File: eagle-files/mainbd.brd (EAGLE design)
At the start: 69.1 x 28 mm, 25 parts, among them J1 4328, T1 3904, X1 TSW-102-07-G-S

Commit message: Moving componets around a little bit to better accomidate xaio board
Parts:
- moved L 1.76 mm to (30.6, 1.54)
- moved R5 1.31 mm to (36.4, 5.49)
- moved 3.3V-LDO 1.26 mm to (31.5, 5.58)
- moved R3 1.04 mm to (35.6, 1.49)
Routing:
- net A2: track 11.3 -> 13.7 mm
- net D9: track 3.07 -> 4.37 mm
- net N$1: track 4.51 -> 3.24 mm
- net 5V: track 35.6 -> 36.9 mm
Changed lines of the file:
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@@
 </autorouter>
 <elements>
-<element name="L" library="adafruit" package="CHIP-LED0805" value="Red" x="29.02" y="2.38" smashed="yes" rot="R270"/>
-<element name="R3" library="adafruit" package="M0805" value="1K" x="35.49" y="2.52" smashed="yes" rot="R180">
-<attribute name="NAME" x="36.706" y="5.304" size="1.27" layer="25" rot="R180"/>
+<element name="L" library="adafruit" package="CHIP-LED0805" value="Red" x="30.564046875" y="1.537128125" smashed="yes" rot="R270"/>
+<element name="R3" library="adafruit" package="M0805" value="1K" x="35.58396875" y="1.485784375" smashed="yes" rot="R180">
+<attribute name="NAME" x="36.79996875" y="4.269784375" size="1.27" layer="25" rot="R180"/>
 </element>
 <element name="SV1" library="con-lstb" library_urn="urn:adsk.eagle:library:162" package="MA10-2" package3d_urn="urn:adsk.eagle:package:8331/1" value="" x="77.47" y="13.97" smashed="yes" rot="MR270">
@@
 </element>
 <element name="U$2" library="sjm4306_LOGO" package="SJM4306_SMALL_NO_MASK" value="" x="28.45" y="17.6" smashed="yes" rot="R45"/>
-<element name="R5" library="adafruit" package="M0805" value="10K" x="36.05" y="6.75" smashed="yes" rot="R90">
-<attribute name="NAME" x="35.034" y="5.734" size="1.27" layer="25" rot="R90"/>
-<attribute name="VALUE" x="38.336" y="5.734" size="1.27" layer="27" rot="R90"/>
+<element name="R5" library="adafruit" package="M0805" value="10K" x="36.407084375" y="5.490134375" smashed="yes" rot="R90">
+<attribute name="NAME" x="35.391084375" y="4.474134375" size="1.27" layer="25" rot="R90"/>
+<attribute name="VALUE" x="38.693084375" y="4.474134375" size="1.27" layer="27" rot="R90"/>
 </element>
 <element name="U$4" library="mgregg" package="CAP-330" value="CAP-330" x="54.4" y="2.65" smashed="yes" rot="R90"/>
@@
 </element>
 <element name="U$9" library="mgregg" package="SMA-DIODE" value="DIODE-ZENIER-CMSH1-20MLTR13" x="46.5" y="13.25" smashed="yes" rot="R270"/>
-<element name="3.3V-LDO" library="mgregg" package="SOT89-BCE" value="LDO-3.3V-AZ1117CR-3.3TRG1" x="30.612034375" y="6.514896875" smashed="yes" rot="R270">
-<attribute name="NAME" x="33.787034375" y="9.054896875" size="1.27" layer="25" rot="R270"/>
-<attribute name="VALUE" x="25.067134375" y="14.769996875" size="1.27" layer="27" rot="R270"/>
+<element name="3.3V-LDO" library="mgregg" package="SOT89-BCE" value="LDO-3.3V-AZ1117CR-3.3TRG1" x="31.454240625" y="5.578375" smashed="yes" rot="R270">
+<attribute name="NAME" x="34.629240625" y="8.118375" size="1.27" layer="25" rot="R270"/>
+<attribute name="VALUE" x="25.909340625" y="13.833475" size="1.27" layer="27" rot="R270"/>
 </element>
 </elements>
@@
 <wire x1="60.2742" y1="25.6032" x2="60.42" y2="25.5" width="0.1524" layer="16"/>
 <wire x1="46.228" y1="3.2004" x2="45.1612" y2="3.2004" width="0.1524" layer="1"/>
-<wire x1="28.076634375" y1="4.976696875" x2="28.072034375" y2="5.015896875" width="0.1524" layer="1"/>
+<wire x1="28.918840625" y1="4.040175" x2="28.914240625" y2="4.079375" width="0.1524" layer="1"/>
 <wire x1="46.228" y1="3.2004" x2="46.4" y2="3.25" width="0.1524" layer="1"/>
-<wire x1="27.898834375" y1="4.976696875" x2="28.072034375" y2="5.015896875" width="0.1524" layer="1"/>
-<wire x1="28.072034375" y1="5.015896875" x2="27.283615625" y2="5.015896875" width="0.508" layer="1"/>
-<wire x1="27.283615625" y1="5.015896875" x2="25.1263125" y2="7.1732" width="0.508" layer="1"/>
+<wire x1="28.741040625" y1="4.040175" x2="28.914240625" y2="4.079375" width="0.1524" layer="1"/>
+<wire x1="28.914240625" y1="4.079375" x2="28.2201375" y2="4.079375" width="0.508" layer="1"/>
+<wire x1="28.2201375" y1="4.079375" x2="25.1263125" y2="7.1732" width="0.508" layer="1"/>
 <wire x1="25.1263125" y1="9.6738875" x2="25.0983" y2="9.7019" width="0.508" layer="1"/>
 <via x="25.0983" y="9.7019" extent="1-16" drill="0.35"/>
@@
 <contactref element="L" pad="A"/>
 <contactref element="U$7" pad="P$8"/>
-<wire x1="27.9146" y1="3.7338" x2="27.9146" y2="2.4892" width="0.1524" layer="1"/>
-<wire x1="27.0256" y1="4.6228" x2="27.9146" y2="3.7338" width="0.1524" layer="16"/>
-<wire x1="27.0256" y1="4.8006" x2="27.0256" y2="4.6228" width="0.1524" layer="16"/>
+<wire x1="27.0256" y1="2.46931875" x2="27.259553125" y2="2.235365625" width="0.1524" layer="16"/>
+<wire x1="27.0256" y1="4.8006" x2="27.0256" y2="2.46931875" width="0.1524" layer="16"/>
 <wire x1="21.5138" y1="10.3124" x2="27.0256" y2="4.8006" width="0.1524" layer="16"/>
 <wire x1="20.9804" y1="10.3124" x2="21.5138" y2="10.3124" width="0.1524" layer="16"/>
-<wire x1="27.9146" y1="2.4892" x2="27.97" y2="2.38" width="0.1524" layer="1"/>
+<wire x1="27.259553125" y1="2.235365625" x2="28.008365625" y2="2.235365625" width="0.1524" layer="1"/>
+<wire x1="28.706603125" y1="1.537128125" x2="28.008365625" y2="2.235365625" width="0.1524" layer="1"/>
+<wire x1="29.514046875" y1="1.537128125" x2="28.706603125" y2="1.537128125" width="0.1524" layer="1"/>
 <wire x1="20.9804" y1="10.3124" x2="20.85" y2="10.46" width="0.1524" layer="16"/>
-<via x="27.9146" y="3.7338" extent="1-16" drill="0.35"/>
+<via x="27.259553125" y="2.235365625" extent="1-16" drill="0.35"/>
 </signal>
 <signal name="D2">
@@
 <contactref element="L" pad="C"/>
 <contactref element="R3" pad="2"/>
-<wire x1="34.4932" y1="2.4892" x2="30.226" y2="2.4892" width="0.1524" layer="1"/>
-<wire x1="30.226" y1="2.4892" x2="30.07" y2="2.38" width="0.1524" layer="1"/>
-<wire x1="34.4932" y1="2.4892" x2="34.54" y2="2.52" width="0.1524" layer="1"/>
+<wire x1="34.052178125" y1="1.86866875" x2="32.087678125" y2="1.86866875" width="0.1524" layer="1"/>
+<wire x1="32.087678125" y1="1.86866875" x2="31.614046875" y2="1.537128125" width="0.1524" layer="1"/>
+<wire x1="34.052178125" y1="1.86866875" x2="34.63396875" y2="1.485784375" width="0.1524" layer="1"/>
 </signal>
 <signal name="G1">
@@
 <contactref element="R5" pad="2"/>
 <contactref element="U$7" pad="P$7"/>
-<wire x1="36.0934" y1="9.0678" x2="36.0934" y2="7.8232" width="0.1524" layer="1"/>
+<wire x1="36.0934" y1="9.0678" x2="36.0934" y2="7.33059375" width="0.1524" layer="1"/>
 <wire x1="36.449" y1="9.4234" x2="36.0934" y2="9.0678" width="0.1524" layer="1"/>
 <wire x1="36.449" y1="9.9568" x2="36.449" y2="9.4234" width="0.1524" layer="1"/>
 <wire x1="36.0934" y1="10.3124" x2="36.449" y2="9.9568" width="0.1524" layer="1"/>
-<wire x1="36.0934" y1="7.8232" x2="36.05" y2="7.7" width="0.1524" layer="1"/>
+<wire x1="36.0934" y1="7.33059375" x2="36.407084375" y2="6.440134375" width="0.1524" layer="1"/>
 <wire x1="36.0934" y1="10.3124" x2="36.05" y2="10.46" width="0.1524" layer="1"/>
 </signal>
@@
 <contactref element="R5" pad="1"/>
 <contactref element="." pad="B"/>
-<wire x1="37.338" y1="5.8674" x2="36.0934" y2="5.8674" width="0.1524" layer="1"/>
+<wire x1="37.338" y1="5.8674" x2="37.261734375" y2="5.8674" width="0.1524" layer="1"/>
 <wire x1="38.9382" y1="4.2672" x2="37.338" y2="5.8674" width="0.1524" layer="1"/>
 <wire x1="38.9382" y1="3.0226" x2="38.9382" y2="4.2672" width="0.1524" layer="1"/>
-<wire x1="36.0934" y1="5.8674" x2="36.05" y2="5.8" width="0.1524" layer="1"/>
+<wire x1="37.261734375" y1="5.8674" x2="36.407084375" y2="4.540134375" width="0.1524" layer="1"/>
 <wire x1="38.9382" y1="3.0226" x2="38.951" y2="2.96" width="0.1524" layer="1"/>
 </signal>
@@
 <wire x1="38.5826" y1="19.7358" x2="37.8714" y2="20.447" width="0.1524" layer="1"/>
 <wire x1="41.9608" y1="19.7358" x2="38.5826" y2="19.7358" width="0.1524" layer="1"/>
-<wire x1="29.8704" y1="7.112" x2="29.66126875" y2="7.112" width="0.1524" layer="1"/>
-<wire x1="34.671" y1="11.9126" x2="29.8704" y2="7.112" width="0.1524" layer="1"/>
-<wire x1="34.671" y1="19.0246" x2="34.671" y2="11.9126" width="0.1524" layer="1"/>
+<wire x1="34.671" y1="10.42773125" x2="29.82164375" y2="5.578375" width="0.1524" layer="1"/>
+<wire x1="29.727240625" y1="5.578375" x2="29.82164375" y2="5.578375" width="0.1524" layer="1"/>
+<wire x1="34.671" y1="19.0246" x2="34.671" y2="10.42773125" width="0.1524" layer="1"/>
 <wire x1="36.0934" y1="20.447" x2="34.671" y2="19.0246" width="0.1524" layer="1"/>
-<wire x1="29.66126875" y1="7.112" x2="28.885034375" y2="6.514896875" width="0.1524" layer="1"/>
 <wire x1="36.0934" y1="20.447" x2="36.05" y2="20.62" width="0.1524" layer="1"/>
 </signal>

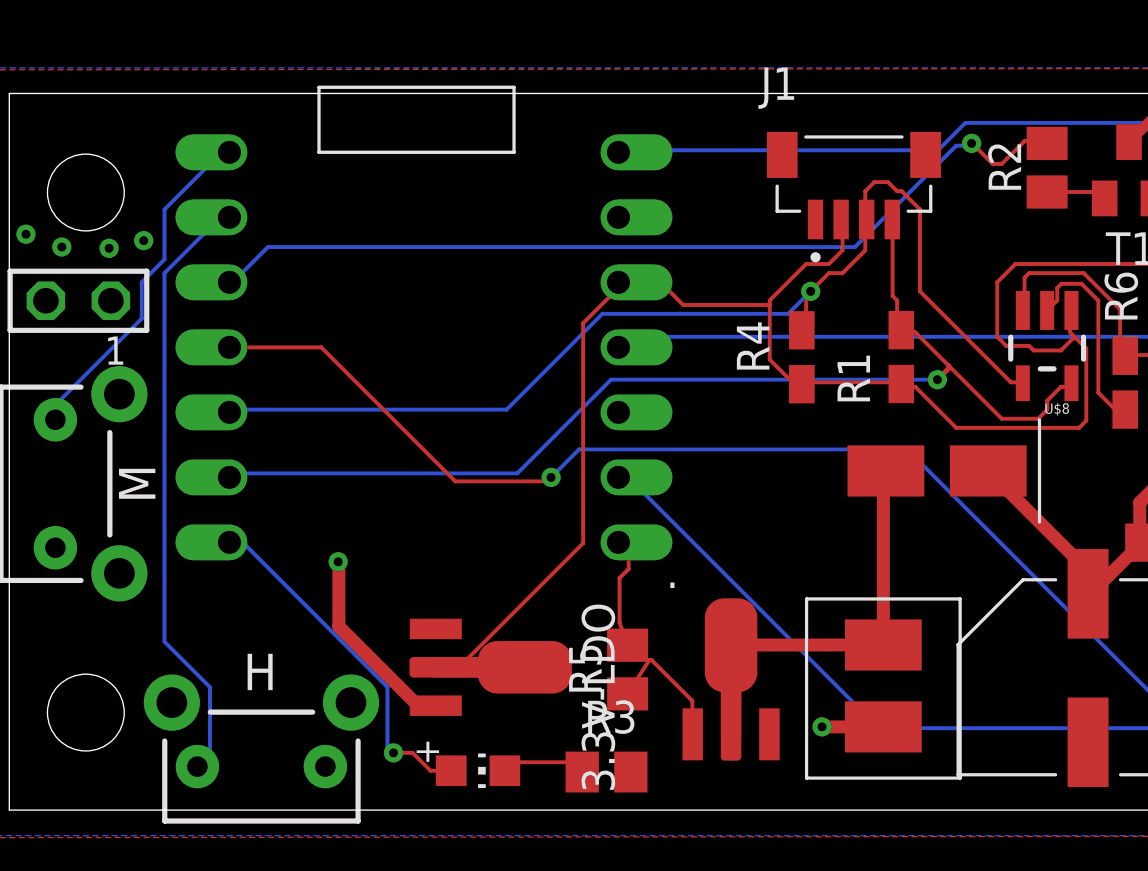
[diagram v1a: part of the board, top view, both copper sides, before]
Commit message: Statring work on adding IV-18 support
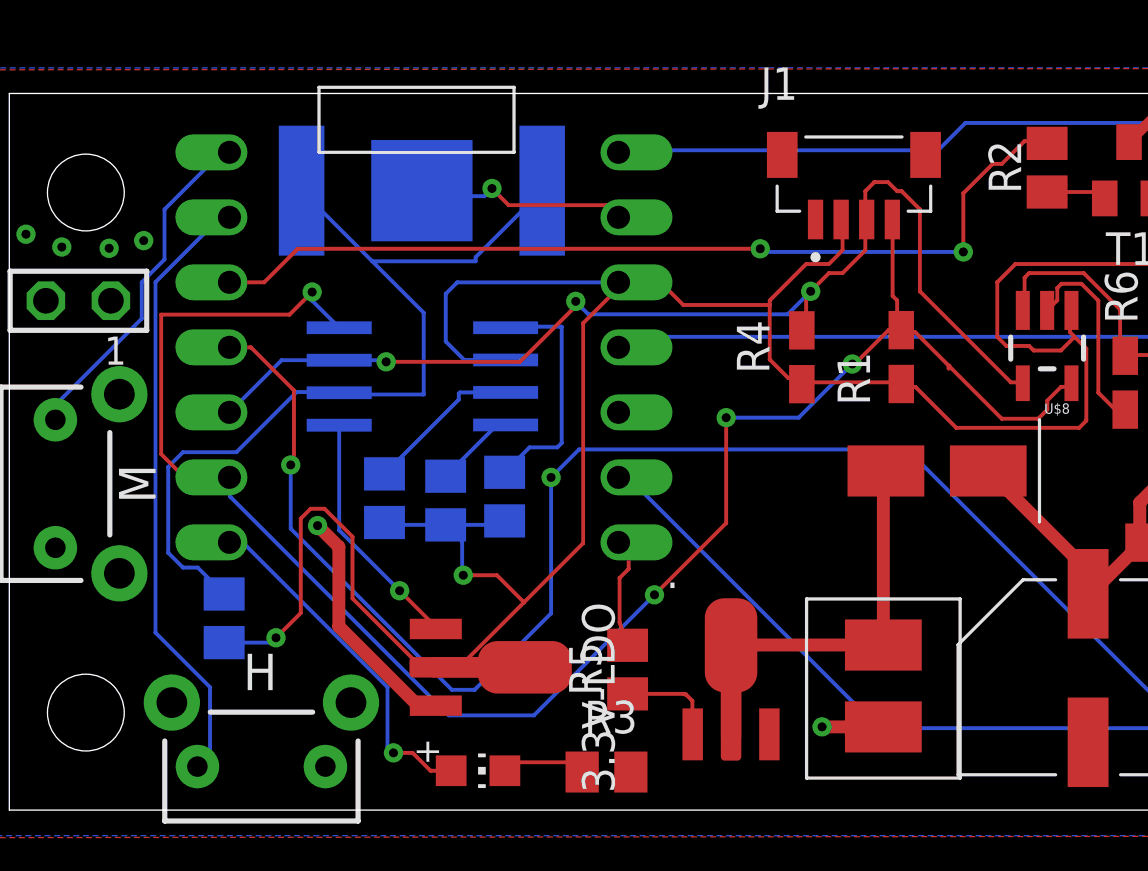
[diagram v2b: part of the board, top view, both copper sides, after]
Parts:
- added R10, R8, R9: 10k, rcl:M0805
- added R11: 0, rcl:M0805
- added U$3: DS3231M, mgregg:SOIC8
- added U$5: BATTERY-2998-COIN, mgregg:BATTERY-2998-COIN
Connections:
- new net N$10: R9.2, U$3.3
- new net N$14: R8.2, U$3.1
- new net N$9: R10.2, U$3.4
- new net RTC-BAT: R11.1, U$3.6, U$5.P$2, U$5.P$3
- net 3V3: now also R10.1, R11.2, R8.1, R9.1, U$3.2
- net GND: now also U$3.5, U$5.P$1
- net SCL: now also U$3.8
- net SDA: now also U$3.7
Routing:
- net 3V3: track 75.2 -> 114.0 mm, vias 0 -> 2
- net RTC-BAT: track 0.00 -> 35.3 mm
- net SCL: track 43.4 -> 69.6 mm, vias 1 -> 4
- net GND: track 7.91 -> 25.8 mm, vias 4 -> 6
- net D10: track 56.0 -> 69.2 mm, vias 2 -> 3
- net N$14: track 0.00 -> 9.46 mm
- net N$10: track 0.00 -> 6.19 mm
- net N$9: track 0.00 -> 3.17 mm
- net 5V: track 36.9 -> 38.6 mm
- net N$2: track 5.23 -> 3.95 mm
- net D2: track 34.9 -> 35.9 mm, vias 1 -> 2
- net SDA: track 42.9 -> 43.8 mm, vias 1 -> 3

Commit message: Adding cam file for production
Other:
- board text added: "BAT-DISABLE"
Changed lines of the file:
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@@
 </polygon>
 <text x="79.9" y="25.7" size="0.8128" layer="21" rot="SR270">V</text>
-<polygon width="0.1524" layer="29">
-<vertex x="42.1" y="9"/>
-<vertex x="42.1" y="11.2"/>
-<vertex x="45.6" y="11.2"/>
-<vertex x="45.6" y="9"/>
-</polygon>
 <text x="67.5" y="26.1" size="0.8128" layer="22" rot="MR0">090919</text>
 <text x="80.7" y="1.4" size="0.8128" layer="21" rot="R180">VFDclock v2.0</text>
 <hole x="15.24" y="24.13" drill="3"/>
 <hole x="15.24" y="3.81" drill="3"/>
+<text x="22.876703125" y="18.369221875" size="1.016" layer="22" rot="MR270">BAT-DISABLE</text>
+<rectangle x1="44.90289375" y1="6.78805625" x2="47.89351875" y2="8.5721" layer="1"/>
+<rectangle x1="44.81589375" y1="6.690153125" x2="48.00226875" y2="8.6156125" layer="29"/>
+<rectangle x1="44.794440625" y1="1.3006875" x2="48.01389375" y2="2.39683125" layer="29"/>
+<rectangle x1="44.90455" y1="1.33215625" x2="47.8985375" y2="2.27095625" layer="1"/>
 </plain>
 <attributes>
